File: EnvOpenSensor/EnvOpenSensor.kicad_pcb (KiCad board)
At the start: 2 copper layers, 89.7 x 67.5 mm, 76 parts, among them IC1 IS31FL3730-QFLS2-TR, IC2 IS31FL3730-QFLS2-TR, IC3 IS31FL3730-QFLS2-TR, IC4 IS31FL3730-QFLS2-TR, J1 HRO_TYPE-C-31-M-12, J2 AVR-ISP-6, SW1 SW_Push, SW2 SW_Push, SW3 SW_Push, SW4 SW_Push, U0 TCA9548ARGER, U1 SCD41-D-R2, U2 Si7021-A20, U4 ATtiny85-20S, U5 TPS63001DRCR

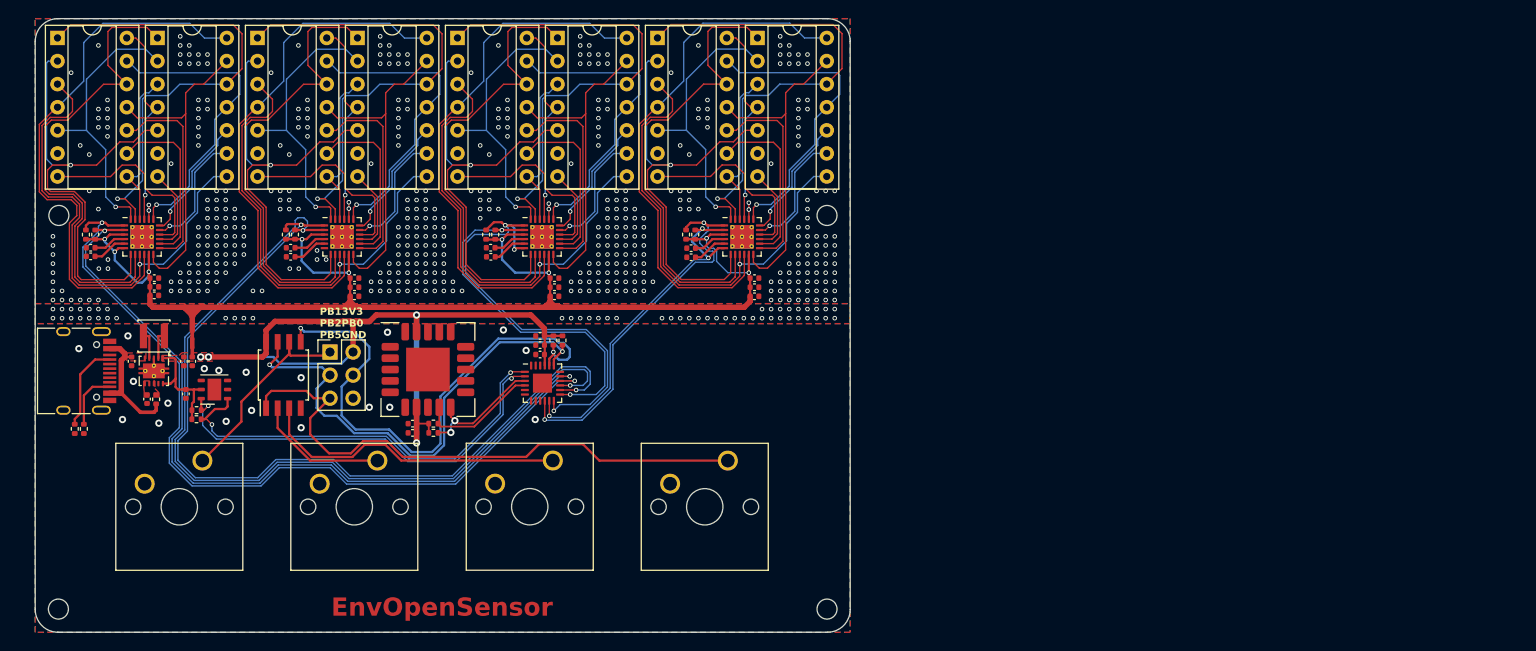
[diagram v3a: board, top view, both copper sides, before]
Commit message: recognised issues with the design, redid schematic to include onboard LEDs and a RP2040, started re-work on PCB
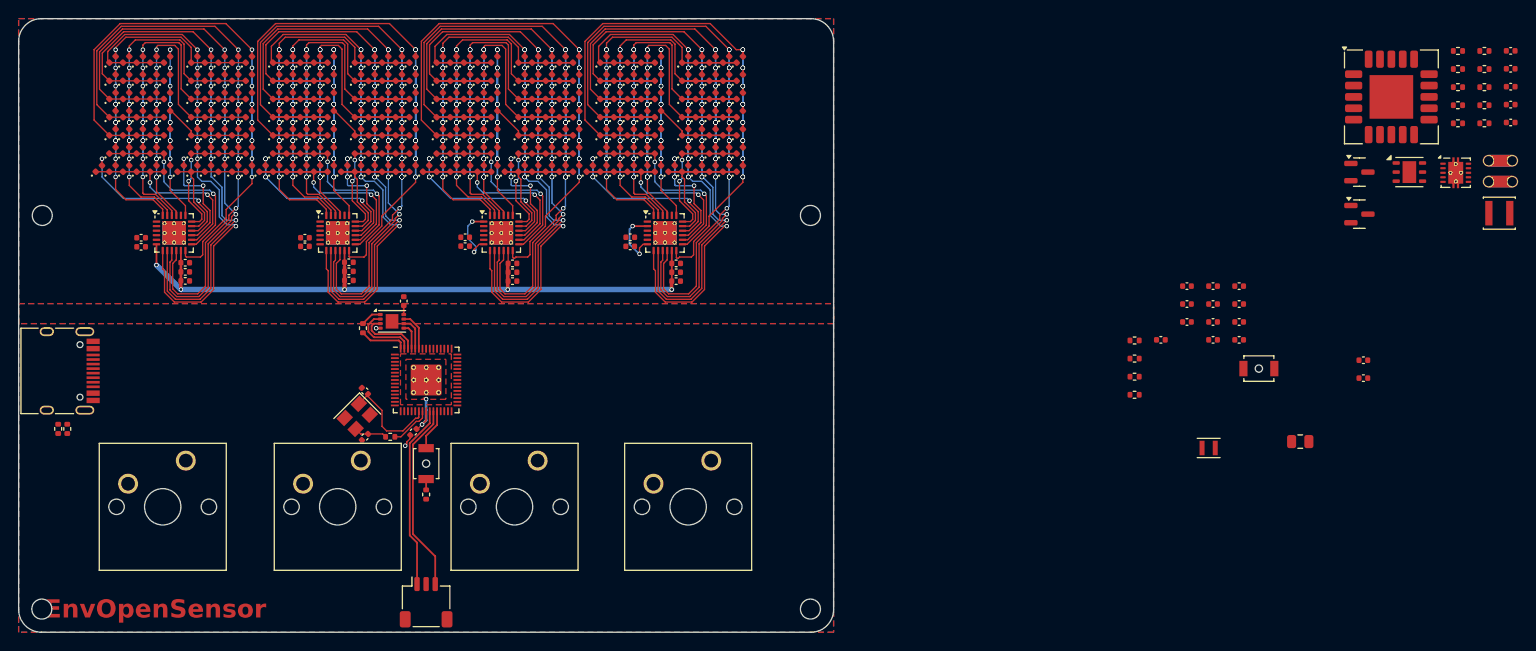
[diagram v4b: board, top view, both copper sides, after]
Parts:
- removed C101, C104, C107, C110: 0402 0.1uF, Capacitor_SMD:C_0402_1005Metric
- removed C102, C105, C108, C111: 0402 1uF, Capacitor_SMD:C_0402_1005Metric
- removed C103, C106, C109, C112: 0402 10uF, Capacitor_SMD:C_0402_1005Metric
- removed DIY-305-1, DIY-305-2, DIY-305-3, DIY-305-4, DIY-305-5, DIY-305-6, DIY-305-7, DIY-305-8: Dip-14 Socket, Package_DIP:DIP-14_W7.62mm_Socket
- removed NT0: NetTie_2, NetTie:NetTie-2_SMD_Pad0.5mm
- removed R101, R102, R103, R104, R105, R106, R107, R108, R14, R15, R16: 10K 0402, Resistor_SMD:R_0402_1005Metric
- removed U0: TCA9548ARGER, Package_DFN_QFN:Texas_RGE0024C_EP2.1x2.1mm
- added C19: 0402 0.1uF, Capacitor_SMD:C_0402_1005Metric, F.Cu at (62.3, 37.5)
- added C20: 0402 0.22uF, Capacitor_SMD:C_0402_1005Metric, F.Cu at (62.3, 36.5)
- added C21: 0402 1uF, Capacitor_SMD:C_0402_1005Metric, F.Cu at (67.5, 40.4)
- added C22: 0402 10uF, Capacitor_SMD:C_0402_1005Metric, F.Cu at (67.5, 41.4)
- added C23: 0402 0.1uF, Capacitor_SMD:C_0402_1005Metric, F.Cu at (85.5, 39.4)
- added C24: 0402 0.1uF, Capacitor_SMD:C_0402_1005Metric, F.Cu at (80.5, 37.5)
- added C25: 0402 0.22uF, Capacitor_SMD:C_0402_1005Metric, F.Cu at (80.5, 36.5)
- added C26: 0402 1uF, Capacitor_SMD:C_0402_1005Metric, F.Cu at (85.5, 40.4)
- added C27: 0402 10uF, Capacitor_SMD:C_0402_1005Metric, F.Cu at (85.5, 41.4)
- added C28: 15pf 0402, Capacitor_SMD:C_0402_1005Metric, F.Cu at (51.3, 53.5)
- added C29: 15pf 0402, Capacitor_SMD:C_0402_1005Metric, F.Cu at (51.3, 58.5)
- added C30: 100nf 0402, Capacitor_SMD:C_0402_1005Metric, F.Cu at (55.5, 43.6)
- added C31: 4.7uf 0402, Capacitor_SMD:C_0402_1005Metric, F.Cu at (138.8, 47.8)
- added C32: 4.7uf 0402, Capacitor_SMD:C_0402_1005Metric, F.Cu at (141.7, 41.9)
- added C33: 100nf 0402, Capacitor_SMD:C_0402_1005Metric, F.Cu at (141.7, 43.9)
- added C34: 4.7uf 0402, Capacitor_SMD:C_0402_1005Metric, F.Cu at (141.7, 45.9)
- added C35: 4.7uf 0402, Capacitor_SMD:C_0402_1005Metric, F.Cu at (56.6, 58.0)
- added C36: 100nf 0402, Capacitor_SMD:C_0402_1005Metric, F.Cu at (144.6, 41.9)
- added C37: 100nf 0402, Capacitor_SMD:C_0402_1005Metric, F.Cu at (144.6, 43.9)
- added C38: 100nf 0402, Capacitor_SMD:C_0402_1005Metric, F.Cu at (144.6, 45.9)
- added C39: 100nf 0402, Capacitor_SMD:C_0402_1005Metric, F.Cu at (144.6, 47.8)
- added C40: 100nf 0402, Capacitor_SMD:C_0402_1005Metric, F.Cu at (147.4, 41.9)
- added C41: 100nf 0402, Capacitor_SMD:C_0402_1005Metric, F.Cu at (147.4, 43.9)
- added C42: 100nf 0402, Capacitor_SMD:C_0402_1005Metric, F.Cu at (147.4, 45.9)
- added C43: 100nf 0402, Capacitor_SMD:C_0402_1005Metric, F.Cu at (147.4, 47.8)
- added C44: 10uf 0805, Capacitor_SMD:C_0805_2012Metric, F.Cu at (154.2, 59.0)
- added D1: LED 0402 10mA, LED_SMD:LED_0402_1005Metric, F.Cu at (22.0, 29.0)
- added D10: LED 0402 10mA, LED_SMD:LED_0402_1005Metric, F.Cu at (25.0, 19.0)
- added D100: LED 0402 10mA, LED_SMD:LED_0402_1005Metric, F.Cu at (46.0, 27.0)
- added D101: LED 0402 10mA, LED_SMD:LED_0402_1005Metric, F.Cu at (46.0, 29.0)
- added D102: LED 0402 10mA, LED_SMD:LED_0402_1005Metric, F.Cu at (47.5, 17.0)
- added D103: LED 0402 10mA, LED_SMD:LED_0402_1005Metric, F.Cu at (47.5, 19.0)
- added D104: LED 0402 10mA, LED_SMD:LED_0402_1005Metric, F.Cu at (47.5, 21.0)
- added D105: LED 0402 10mA, LED_SMD:LED_0402_1005Metric, F.Cu at (47.5, 23.0)
- added D106: LED 0402 10mA, LED_SMD:LED_0402_1005Metric, F.Cu at (47.5, 25.0)
- added D107: LED 0402 10mA, LED_SMD:LED_0402_1005Metric, F.Cu at (47.5, 27.0)
- added D108: LED 0402 10mA, LED_SMD:LED_0402_1005Metric, F.Cu at (47.5, 29.0)
- added D109: LED 0402 10mA, LED_SMD:LED_0402_1005Metric, F.Cu at (49.0, 29.0)
- added D11: LED 0402 10mA, LED_SMD:LED_0402_1005Metric, F.Cu at (25.0, 21.0)
- added D110: LED 0402 10mA, LED_SMD:LED_0402_1005Metric, F.Cu at (50.5, 17.0)
- added D111: LED 0402 10mA, LED_SMD:LED_0402_1005Metric, F.Cu at (50.5, 19.0)
- added D112: LED 0402 10mA, LED_SMD:LED_0402_1005Metric, F.Cu at (50.5, 21.0)
- added D113: LED 0402 10mA, LED_SMD:LED_0402_1005Metric, F.Cu at (50.5, 23.0)
- added D114: LED 0402 10mA, LED_SMD:LED_0402_1005Metric, F.Cu at (50.5, 25.0)
- added D115: LED 0402 10mA, LED_SMD:LED_0402_1005Metric, F.Cu at (50.5, 27.0)
- added D116: LED 0402 10mA, LED_SMD:LED_0402_1005Metric, F.Cu at (50.5, 29.0)
- added D117: LED 0402 10mA, LED_SMD:LED_0402_1005Metric, F.Cu at (52.0, 17.0)
- added D118: LED 0402 10mA, LED_SMD:LED_0402_1005Metric, F.Cu at (52.0, 19.0)
- added D119: LED 0402 10mA, LED_SMD:LED_0402_1005Metric, F.Cu at (52.0, 21.0)
- added D12: LED 0402 10mA, LED_SMD:LED_0402_1005Metric, F.Cu at (25.0, 23.0)
- added D120: LED 0402 10mA, LED_SMD:LED_0402_1005Metric, F.Cu at (52.0, 23.0)
- added D121: LED 0402 10mA, LED_SMD:LED_0402_1005Metric, F.Cu at (52.0, 25.0)
- added D122: LED 0402 10mA, LED_SMD:LED_0402_1005Metric, F.Cu at (52.0, 27.0)
- added D123: LED 0402 10mA, LED_SMD:LED_0402_1005Metric, F.Cu at (52.0, 29.0)
- added D124: LED 0402 10mA, LED_SMD:LED_0402_1005Metric, F.Cu at (53.5, 17.0)
- added D125: LED 0402 10mA, LED_SMD:LED_0402_1005Metric, F.Cu at (53.5, 19.0)
- added D126: LED 0402 10mA, LED_SMD:LED_0402_1005Metric, F.Cu at (53.5, 21.0)
- added D127: LED 0402 10mA, LED_SMD:LED_0402_1005Metric, F.Cu at (53.5, 23.0)
- added D128: LED 0402 10mA, LED_SMD:LED_0402_1005Metric, F.Cu at (53.5, 25.0)
- added D129: LED 0402 10mA, LED_SMD:LED_0402_1005Metric, F.Cu at (53.5, 27.0)
- added D13: LED 0402 10mA, LED_SMD:LED_0402_1005Metric, F.Cu at (25.0, 25.0)
- added D130: LED 0402 10mA, LED_SMD:LED_0402_1005Metric, F.Cu at (53.5, 29.0)
- added D131: LED 0402 10mA, LED_SMD:LED_0402_1005Metric, F.Cu at (55.0, 17.0)
- added D132: LED 0402 10mA, LED_SMD:LED_0402_1005Metric, F.Cu at (55.0, 19.0)
- added D133: LED 0402 10mA, LED_SMD:LED_0402_1005Metric, F.Cu at (55.0, 21.0)
- added D134: LED 0402 10mA, LED_SMD:LED_0402_1005Metric, F.Cu at (55.0, 23.0)
- added D135: LED 0402 10mA, LED_SMD:LED_0402_1005Metric, F.Cu at (55.0, 25.0)
- added D136: LED 0402 10mA, LED_SMD:LED_0402_1005Metric, F.Cu at (55.0, 27.0)
- added D137: LED 0402 10mA, LED_SMD:LED_0402_1005Metric, F.Cu at (55.0, 29.0)
- added D138: LED 0402 10mA, LED_SMD:LED_0402_1005Metric, F.Cu at (56.5, 17.0)
- added D139: LED 0402 10mA, LED_SMD:LED_0402_1005Metric, F.Cu at (56.5, 19.0)
- added D14: LED 0402 10mA, LED_SMD:LED_0402_1005Metric, F.Cu at (25.0, 27.0)
- added D140: LED 0402 10mA, LED_SMD:LED_0402_1005Metric, F.Cu at (56.5, 21.0)
- added D141: LED 0402 10mA, LED_SMD:LED_0402_1005Metric, F.Cu at (56.5, 23.0)
- added D142: LED 0402 10mA, LED_SMD:LED_0402_1005Metric, F.Cu at (56.5, 25.0)
- added D143: LED 0402 10mA, LED_SMD:LED_0402_1005Metric, F.Cu at (56.5, 27.0)
- added D144: LED 0402 10mA, LED_SMD:LED_0402_1005Metric, F.Cu at (56.5, 29.0)
- added D145: LED 0402 10mA, LED_SMD:LED_0402_1005Metric, F.Cu at (58.0, 29.0)
- added D146: LED 0402 10mA, LED_SMD:LED_0402_1005Metric, F.Cu at (59.5, 17.0)
- added D147: LED 0402 10mA, LED_SMD:LED_0402_1005Metric, F.Cu at (59.5, 19.0)
- added D148: LED 0402 10mA, LED_SMD:LED_0402_1005Metric, F.Cu at (59.5, 21.0)
- added D149: LED 0402 10mA, LED_SMD:LED_0402_1005Metric, F.Cu at (59.5, 23.0)
- added D15: LED 0402 10mA, LED_SMD:LED_0402_1005Metric, F.Cu at (25.0, 29.0)
- added D150: LED 0402 10mA, LED_SMD:LED_0402_1005Metric, F.Cu at (59.5, 25.0)
- added D151: LED 0402 10mA, LED_SMD:LED_0402_1005Metric, F.Cu at (59.5, 27.0)
- added D152: LED 0402 10mA, LED_SMD:LED_0402_1005Metric, F.Cu at (59.5, 29.0)
- added D153: LED 0402 10mA, LED_SMD:LED_0402_1005Metric, F.Cu at (61.0, 17.0)
- added D154: LED 0402 10mA, LED_SMD:LED_0402_1005Metric, F.Cu at (61.0, 19.0)
- added D155: LED 0402 10mA, LED_SMD:LED_0402_1005Metric, F.Cu at (61.0, 21.0)
- added D156: LED 0402 10mA, LED_SMD:LED_0402_1005Metric, F.Cu at (61.0, 23.0)
- added D157: LED 0402 10mA, LED_SMD:LED_0402_1005Metric, F.Cu at (61.0, 25.0)
- added D158: LED 0402 10mA, LED_SMD:LED_0402_1005Metric, F.Cu at (61.0, 27.0)
- added D159: LED 0402 10mA, LED_SMD:LED_0402_1005Metric, F.Cu at (61.0, 29.0)
- added D16: LED 0402 10mA, LED_SMD:LED_0402_1005Metric, F.Cu at (26.5, 17.0)
- added D160: LED 0402 10mA, LED_SMD:LED_0402_1005Metric, F.Cu at (62.5, 17.0)
- added D161: LED 0402 10mA, LED_SMD:LED_0402_1005Metric, F.Cu at (62.5, 19.0)
- added D162: LED 0402 10mA, LED_SMD:LED_0402_1005Metric, F.Cu at (62.5, 21.0)
- added D163: LED 0402 10mA, LED_SMD:LED_0402_1005Metric, F.Cu at (62.5, 23.0)
- added D164: LED 0402 10mA, LED_SMD:LED_0402_1005Metric, F.Cu at (62.5, 25.0)
- added D165: LED 0402 10mA, LED_SMD:LED_0402_1005Metric, F.Cu at (62.5, 27.0)
- added D166: LED 0402 10mA, LED_SMD:LED_0402_1005Metric, F.Cu at (62.5, 29.0)
- added D167: LED 0402 10mA, LED_SMD:LED_0402_1005Metric, F.Cu at (64.0, 17.0)
- added D168: LED 0402 10mA, LED_SMD:LED_0402_1005Metric, F.Cu at (64.0, 19.0)
- added D169: LED 0402 10mA, LED_SMD:LED_0402_1005Metric, F.Cu at (64.0, 21.0)
- added D17: LED 0402 10mA, LED_SMD:LED_0402_1005Metric, F.Cu at (26.5, 19.0)
- added D170: LED 0402 10mA, LED_SMD:LED_0402_1005Metric, F.Cu at (64.0, 23.0)
- added D171: LED 0402 10mA, LED_SMD:LED_0402_1005Metric, F.Cu at (64.0, 25.0)
- added D172: LED 0402 10mA, LED_SMD:LED_0402_1005Metric, F.Cu at (64.0, 27.0)
- added D173: LED 0402 10mA, LED_SMD:LED_0402_1005Metric, F.Cu at (64.0, 29.0)
- added D174: LED 0402 10mA, LED_SMD:LED_0402_1005Metric, F.Cu at (65.5, 17.0)
- added D175: LED 0402 10mA, LED_SMD:LED_0402_1005Metric, F.Cu at (65.5, 19.0)
- added D176: LED 0402 10mA, LED_SMD:LED_0402_1005Metric, F.Cu at (65.5, 21.0)
- added D177: LED 0402 10mA, LED_SMD:LED_0402_1005Metric, F.Cu at (65.5, 23.0)
- added D178: LED 0402 10mA, LED_SMD:LED_0402_1005Metric, F.Cu at (65.5, 25.0)
- added D179: LED 0402 10mA, LED_SMD:LED_0402_1005Metric, F.Cu at (65.5, 27.0)
- added D18: LED 0402 10mA, LED_SMD:LED_0402_1005Metric, F.Cu at (26.5, 21.0)
- added D180: LED 0402 10mA, LED_SMD:LED_0402_1005Metric, F.Cu at (65.5, 29.0)
- added D181: LED 0402 10mA, LED_SMD:LED_0402_1005Metric, F.Cu at (67.0, 29.0)
- added D182: LED 0402 10mA, LED_SMD:LED_0402_1005Metric, F.Cu at (68.5, 17.0)
- added D183: LED 0402 10mA, LED_SMD:LED_0402_1005Metric, F.Cu at (68.5, 19.0)
- added D184: LED 0402 10mA, LED_SMD:LED_0402_1005Metric, F.Cu at (68.5, 21.0)
- added D185: LED 0402 10mA, LED_SMD:LED_0402_1005Metric, F.Cu at (68.5, 23.0)
- added D186: LED 0402 10mA, LED_SMD:LED_0402_1005Metric, F.Cu at (68.5, 25.0)
- added D187: LED 0402 10mA, LED_SMD:LED_0402_1005Metric, F.Cu at (68.5, 27.0)
- added D188: LED 0402 10mA, LED_SMD:LED_0402_1005Metric, F.Cu at (68.5, 29.0)
- added D189: LED 0402 10mA, LED_SMD:LED_0402_1005Metric, F.Cu at (70.0, 17.0)
- added D19: LED 0402 10mA, LED_SMD:LED_0402_1005Metric, F.Cu at (26.5, 23.0)
- added D190: LED 0402 10mA, LED_SMD:LED_0402_1005Metric, F.Cu at (70.0, 19.0)
- added D191: LED 0402 10mA, LED_SMD:LED_0402_1005Metric, F.Cu at (70.0, 21.0)
- added D192: LED 0402 10mA, LED_SMD:LED_0402_1005Metric, F.Cu at (70.0, 23.0)
- added D193: LED 0402 10mA, LED_SMD:LED_0402_1005Metric, F.Cu at (70.0, 25.0)
- added D194: LED 0402 10mA, LED_SMD:LED_0402_1005Metric, F.Cu at (70.0, 27.0)
- added D195: LED 0402 10mA, LED_SMD:LED_0402_1005Metric, F.Cu at (70.0, 29.0)
- added D196: LED 0402 10mA, LED_SMD:LED_0402_1005Metric, F.Cu at (71.5, 17.0)
- added D197: LED 0402 10mA, LED_SMD:LED_0402_1005Metric, F.Cu at (71.5, 19.0)
- added D198: LED 0402 10mA, LED_SMD:LED_0402_1005Metric, F.Cu at (71.5, 21.0)
- added D199: LED 0402 10mA, LED_SMD:LED_0402_1005Metric, F.Cu at (71.5, 23.0)
- added D2: LED 0402 10mA, LED_SMD:LED_0402_1005Metric, F.Cu at (23.5, 17.0)
- added D20: LED 0402 10mA, LED_SMD:LED_0402_1005Metric, F.Cu at (26.5, 25.0)
- added D200: LED 0402 10mA, LED_SMD:LED_0402_1005Metric, F.Cu at (71.5, 25.0)
- added D201: LED 0402 10mA, LED_SMD:LED_0402_1005Metric, F.Cu at (71.5, 27.0)
- added D202: LED 0402 10mA, LED_SMD:LED_0402_1005Metric, F.Cu at (71.5, 29.0)
- added D203: LED 0402 10mA, LED_SMD:LED_0402_1005Metric, F.Cu at (73.0, 17.0)
- added D204: LED 0402 10mA, LED_SMD:LED_0402_1005Metric, F.Cu at (73.0, 19.0)
- added D205: LED 0402 10mA, LED_SMD:LED_0402_1005Metric, F.Cu at (73.0, 21.0)
- added D206: LED 0402 10mA, LED_SMD:LED_0402_1005Metric, F.Cu at (73.0, 23.0)
- added D207: LED 0402 10mA, LED_SMD:LED_0402_1005Metric, F.Cu at (73.0, 25.0)
- added D208: LED 0402 10mA, LED_SMD:LED_0402_1005Metric, F.Cu at (73.0, 27.0)
- added D209: LED 0402 10mA, LED_SMD:LED_0402_1005Metric, F.Cu at (73.0, 29.0)
- added D21: LED 0402 10mA, LED_SMD:LED_0402_1005Metric, F.Cu at (26.5, 27.0)
- added D210: LED 0402 10mA, LED_SMD:LED_0402_1005Metric, F.Cu at (74.5, 17.0)
- added D211: LED 0402 10mA, LED_SMD:LED_0402_1005Metric, F.Cu at (74.5, 19.0)
- added D212: LED 0402 10mA, LED_SMD:LED_0402_1005Metric, F.Cu at (74.5, 21.0)
- added D213: LED 0402 10mA, LED_SMD:LED_0402_1005Metric, F.Cu at (74.5, 23.0)
- added D214: LED 0402 10mA, LED_SMD:LED_0402_1005Metric, F.Cu at (74.5, 25.0)
- added D215: LED 0402 10mA, LED_SMD:LED_0402_1005Metric, F.Cu at (74.5, 27.0)
- added D216: LED 0402 10mA, LED_SMD:LED_0402_1005Metric, F.Cu at (74.5, 29.0)
- added D217: LED 0402 10mA, LED_SMD:LED_0402_1005Metric, F.Cu at (76.0, 29.0)
- added D218: LED 0402 10mA, LED_SMD:LED_0402_1005Metric, F.Cu at (77.5, 17.0)
- added D219: LED 0402 10mA, LED_SMD:LED_0402_1005Metric, F.Cu at (77.5, 19.0)
- added D22: LED 0402 10mA, LED_SMD:LED_0402_1005Metric, F.Cu at (26.5, 29.0)
- added D220: LED 0402 10mA, LED_SMD:LED_0402_1005Metric, F.Cu at (77.5, 21.0)
- added D221: LED 0402 10mA, LED_SMD:LED_0402_1005Metric, F.Cu at (77.5, 23.0)
- added D222: LED 0402 10mA, LED_SMD:LED_0402_1005Metric, F.Cu at (77.5, 25.0)
- added D223: LED 0402 10mA, LED_SMD:LED_0402_1005Metric, F.Cu at (77.5, 27.0)
- added D224: LED 0402 10mA, LED_SMD:LED_0402_1005Metric, F.Cu at (77.5, 29.0)
- added D225: LED 0402 10mA, LED_SMD:LED_0402_1005Metric, F.Cu at (79.0, 17.0)
- added D226: LED 0402 10mA, LED_SMD:LED_0402_1005Metric, F.Cu at (79.0, 19.0)
- added D227: LED 0402 10mA, LED_SMD:LED_0402_1005Metric, F.Cu at (79.0, 21.0)
- added D228: LED 0402 10mA, LED_SMD:LED_0402_1005Metric, F.Cu at (79.0, 23.0)
- added D229: LED 0402 10mA, LED_SMD:LED_0402_1005Metric, F.Cu at (79.0, 25.0)
- added D23: LED 0402 10mA, LED_SMD:LED_0402_1005Metric, F.Cu at (28.0, 17.0)
- added D230: LED 0402 10mA, LED_SMD:LED_0402_1005Metric, F.Cu at (79.0, 27.0)
- added D231: LED 0402 10mA, LED_SMD:LED_0402_1005Metric, F.Cu at (79.0, 29.0)
- added D232: LED 0402 10mA, LED_SMD:LED_0402_1005Metric, F.Cu at (80.5, 17.0)
- added D233: LED 0402 10mA, LED_SMD:LED_0402_1005Metric, F.Cu at (80.5, 19.0)
- added D234: LED 0402 10mA, LED_SMD:LED_0402_1005Metric, F.Cu at (80.5, 21.0)
- added D235: LED 0402 10mA, LED_SMD:LED_0402_1005Metric, F.Cu at (80.5, 23.0)
- added D236: LED 0402 10mA, LED_SMD:LED_0402_1005Metric, F.Cu at (80.5, 25.0)
- added D237: LED 0402 10mA, LED_SMD:LED_0402_1005Metric, F.Cu at (80.5, 27.0)
- added D238: LED 0402 10mA, LED_SMD:LED_0402_1005Metric, F.Cu at (80.5, 29.0)
- added D239: LED 0402 10mA, LED_SMD:LED_0402_1005Metric, F.Cu at (82.0, 17.0)
- added D24: LED 0402 10mA, LED_SMD:LED_0402_1005Metric, F.Cu at (28.0, 19.0)
- added D240: LED 0402 10mA, LED_SMD:LED_0402_1005Metric, F.Cu at (82.0, 19.0)
- added D241: LED 0402 10mA, LED_SMD:LED_0402_1005Metric, F.Cu at (82.0, 21.0)
- added D242: LED 0402 10mA, LED_SMD:LED_0402_1005Metric, F.Cu at (82.0, 23.0)
- added D243: LED 0402 10mA, LED_SMD:LED_0402_1005Metric, F.Cu at (82.0, 25.0)
- added D244: LED 0402 10mA, LED_SMD:LED_0402_1005Metric, F.Cu at (82.0, 27.0)
- added D245: LED 0402 10mA, LED_SMD:LED_0402_1005Metric, F.Cu at (82.0, 29.0)
- added D246: LED 0402 10mA, LED_SMD:LED_0402_1005Metric, F.Cu at (83.5, 17.0)
- added D247: LED 0402 10mA, LED_SMD:LED_0402_1005Metric, F.Cu at (83.5, 19.0)
- added D248: LED 0402 10mA, LED_SMD:LED_0402_1005Metric, F.Cu at (83.5, 21.0)
- added D249: LED 0402 10mA, LED_SMD:LED_0402_1005Metric, F.Cu at (83.5, 23.0)
- added D25: LED 0402 10mA, LED_SMD:LED_0402_1005Metric, F.Cu at (28.0, 21.0)
- added D250: LED 0402 10mA, LED_SMD:LED_0402_1005Metric, F.Cu at (83.5, 25.0)
- added D251: LED 0402 10mA, LED_SMD:LED_0402_1005Metric, F.Cu at (83.5, 27.0)
- added D252: LED 0402 10mA, LED_SMD:LED_0402_1005Metric, F.Cu at (83.5, 29.0)
- added D253: LED 0402 10mA, LED_SMD:LED_0402_1005Metric, F.Cu at (85.0, 29.0)
- added D254: LED 0402 10mA, LED_SMD:LED_0402_1005Metric, F.Cu at (86.5, 17.0)
- added D255: LED 0402 10mA, LED_SMD:LED_0402_1005Metric, F.Cu at (86.5, 19.0)
- added D256: LED 0402 10mA, LED_SMD:LED_0402_1005Metric, F.Cu at (86.5, 21.0)
- added D257: LED 0402 10mA, LED_SMD:LED_0402_1005Metric, F.Cu at (86.5, 23.0)
- added D258: LED 0402 10mA, LED_SMD:LED_0402_1005Metric, F.Cu at (86.5, 25.0)
- added D259: LED 0402 10mA, LED_SMD:LED_0402_1005Metric, F.Cu at (86.5, 27.0)
- added D26: LED 0402 10mA, LED_SMD:LED_0402_1005Metric, F.Cu at (28.0, 23.0)
- added D260: LED 0402 10mA, LED_SMD:LED_0402_1005Metric, F.Cu at (86.5, 29.0)
- added D261: LED 0402 10mA, LED_SMD:LED_0402_1005Metric, F.Cu at (88.0, 17.0)
- added D262: LED 0402 10mA, LED_SMD:LED_0402_1005Metric, F.Cu at (88.0, 19.0)
- added D263: LED 0402 10mA, LED_SMD:LED_0402_1005Metric, F.Cu at (88.0, 21.0)
- added D264: LED 0402 10mA, LED_SMD:LED_0402_1005Metric, F.Cu at (88.0, 23.0)
- added D265: LED 0402 10mA, LED_SMD:LED_0402_1005Metric, F.Cu at (88.0, 25.0)
- added D266: LED 0402 10mA, LED_SMD:LED_0402_1005Metric, F.Cu at (88.0, 27.0)
- added D267: LED 0402 10mA, LED_SMD:LED_0402_1005Metric, F.Cu at (88.0, 29.0)
- added D268: LED 0402 10mA, LED_SMD:LED_0402_1005Metric, F.Cu at (89.5, 17.0)
- added D269: LED 0402 10mA, LED_SMD:LED_0402_1005Metric, F.Cu at (89.5, 19.0)
- added D27: LED 0402 10mA, LED_SMD:LED_0402_1005Metric, F.Cu at (28.0, 25.0)
- added D270: LED 0402 10mA, LED_SMD:LED_0402_1005Metric, F.Cu at (89.5, 21.0)
- added D271: LED 0402 10mA, LED_SMD:LED_0402_1005Metric, F.Cu at (89.5, 23.0)
- added D272: LED 0402 10mA, LED_SMD:LED_0402_1005Metric, F.Cu at (89.5, 25.0)
- added D273: LED 0402 10mA, LED_SMD:LED_0402_1005Metric, F.Cu at (89.5, 27.0)
- added D274: LED 0402 10mA, LED_SMD:LED_0402_1005Metric, F.Cu at (89.5, 29.0)
- added D275: LED 0402 10mA, LED_SMD:LED_0402_1005Metric, F.Cu at (91.0, 17.0)
- added D276: LED 0402 10mA, LED_SMD:LED_0402_1005Metric, F.Cu at (91.0, 19.0)
- added D277: LED 0402 10mA, LED_SMD:LED_0402_1005Metric, F.Cu at (91.0, 21.0)
- added D278: LED 0402 10mA, LED_SMD:LED_0402_1005Metric, F.Cu at (91.0, 23.0)
- added D279: LED 0402 10mA, LED_SMD:LED_0402_1005Metric, F.Cu at (91.0, 25.0)
- added D28: LED 0402 10mA, LED_SMD:LED_0402_1005Metric, F.Cu at (28.0, 27.0)
- added D280: LED 0402 10mA, LED_SMD:LED_0402_1005Metric, F.Cu at (91.0, 27.0)
- added D281: LED 0402 10mA, LED_SMD:LED_0402_1005Metric, F.Cu at (91.0, 29.0)
- added D282: LED 0402 10mA, LED_SMD:LED_0402_1005Metric, F.Cu at (92.5, 17.0)
- added D283: LED 0402 10mA, LED_SMD:LED_0402_1005Metric, F.Cu at (92.5, 19.0)
- added D284: LED 0402 10mA, LED_SMD:LED_0402_1005Metric, F.Cu at (92.5, 21.0)
- added D285: LED 0402 10mA, LED_SMD:LED_0402_1005Metric, F.Cu at (92.5, 23.0)
- added D286: LED 0402 10mA, LED_SMD:LED_0402_1005Metric, F.Cu at (92.5, 25.0)
- added D287: LED 0402 10mA, LED_SMD:LED_0402_1005Metric, F.Cu at (92.5, 27.0)
- added D288: LED 0402 10mA, LED_SMD:LED_0402_1005Metric, F.Cu at (92.5, 29.0)
- added D29: LED 0402 10mA, LED_SMD:LED_0402_1005Metric, F.Cu at (28.0, 29.0)
- added D3: LED 0402 10mA, LED_SMD:LED_0402_1005Metric, F.Cu at (23.5, 19.0)
- added D30: LED 0402 10mA, LED_SMD:LED_0402_1005Metric, F.Cu at (29.5, 17.0)
- added D31: LED 0402 10mA, LED_SMD:LED_0402_1005Metric, F.Cu at (29.5, 19.0)
- added D32: LED 0402 10mA, LED_SMD:LED_0402_1005Metric, F.Cu at (29.5, 21.0)
- added D33: LED 0402 10mA, LED_SMD:LED_0402_1005Metric, F.Cu at (29.5, 23.0)
- added D34: LED 0402 10mA, LED_SMD:LED_0402_1005Metric, F.Cu at (29.5, 25.0)
- added D35: LED 0402 10mA, LED_SMD:LED_0402_1005Metric, F.Cu at (29.5, 27.0)
- added D36: LED 0402 10mA, LED_SMD:LED_0402_1005Metric, F.Cu at (29.5, 29.0)
- added D37: LED 0402 10mA, LED_SMD:LED_0402_1005Metric, F.Cu at (31.0, 29.0)
- added D38: LED 0402 10mA, LED_SMD:LED_0402_1005Metric, F.Cu at (32.5, 17.0)
- added D39: LED 0402 10mA, LED_SMD:LED_0402_1005Metric, F.Cu at (32.5, 19.0)
- added D4: LED 0402 10mA, LED_SMD:LED_0402_1005Metric, F.Cu at (23.5, 21.0)
- added D40: LED 0402 10mA, LED_SMD:LED_0402_1005Metric, F.Cu at (32.5, 21.0)
- added D41: LED 0402 10mA, LED_SMD:LED_0402_1005Metric, F.Cu at (32.5, 23.0)
- added D42: LED 0402 10mA, LED_SMD:LED_0402_1005Metric, F.Cu at (32.5, 25.0)
- added D43: LED 0402 10mA, LED_SMD:LED_0402_1005Metric, F.Cu at (32.5, 27.0)
- added D44: LED 0402 10mA, LED_SMD:LED_0402_1005Metric, F.Cu at (32.5, 29.0)
- added D45: LED 0402 10mA, LED_SMD:LED_0402_1005Metric, F.Cu at (34.0, 17.0)
- added D46: LED 0402 10mA, LED_SMD:LED_0402_1005Metric, F.Cu at (34.0, 19.0)
- added D47: LED 0402 10mA, LED_SMD:LED_0402_1005Metric, F.Cu at (34.0, 21.0)
- added D48: LED 0402 10mA, LED_SMD:LED_0402_1005Metric, F.Cu at (34.0, 23.0)
- added D49: LED 0402 10mA, LED_SMD:LED_0402_1005Metric, F.Cu at (34.0, 25.0)
- added D5: LED 0402 10mA, LED_SMD:LED_0402_1005Metric, F.Cu at (23.5, 23.0)
- added D50: LED 0402 10mA, LED_SMD:LED_0402_1005Metric, F.Cu at (34.0, 27.0)
- added D51: LED 0402 10mA, LED_SMD:LED_0402_1005Metric, F.Cu at (34.0, 29.0)
- added D52: LED 0402 10mA, LED_SMD:LED_0402_1005Metric, F.Cu at (35.5, 17.0)
- added D53: LED 0402 10mA, LED_SMD:LED_0402_1005Metric, F.Cu at (35.5, 19.0)
- added D54: LED 0402 10mA, LED_SMD:LED_0402_1005Metric, F.Cu at (35.5, 21.0)
- added D55: LED 0402 10mA, LED_SMD:LED_0402_1005Metric, F.Cu at (35.5, 23.0)
- added D56: LED 0402 10mA, LED_SMD:LED_0402_1005Metric, F.Cu at (35.5, 25.0)
- added D57: LED 0402 10mA, LED_SMD:LED_0402_1005Metric, F.Cu at (35.5, 27.0)
- added D58: LED 0402 10mA, LED_SMD:LED_0402_1005Metric, F.Cu at (35.5, 29.0)
- added D59: LED 0402 10mA, LED_SMD:LED_0402_1005Metric, F.Cu at (37.0, 17.0)
- added D6: LED 0402 10mA, LED_SMD:LED_0402_1005Metric, F.Cu at (23.5, 25.0)
- added D60: LED 0402 10mA, LED_SMD:LED_0402_1005Metric, F.Cu at (37.0, 19.0)
- added D61: LED 0402 10mA, LED_SMD:LED_0402_1005Metric, F.Cu at (37.0, 21.0)
- added D62: LED 0402 10mA, LED_SMD:LED_0402_1005Metric, F.Cu at (37.0, 23.0)
- added D63: LED 0402 10mA, LED_SMD:LED_0402_1005Metric, F.Cu at (37.0, 25.0)
- added D64: LED 0402 10mA, LED_SMD:LED_0402_1005Metric, F.Cu at (37.0, 27.0)
- added D65: LED 0402 10mA, LED_SMD:LED_0402_1005Metric, F.Cu at (37.0, 29.0)
- added D66: LED 0402 10mA, LED_SMD:LED_0402_1005Metric, F.Cu at (38.5, 17.0)
- added D67: LED 0402 10mA, LED_SMD:LED_0402_1005Metric, F.Cu at (38.5, 19.0)
- added D68: LED 0402 10mA, LED_SMD:LED_0402_1005Metric, F.Cu at (38.5, 21.0)
- added D69: LED 0402 10mA, LED_SMD:LED_0402_1005Metric, F.Cu at (38.5, 23.0)
- added D7: LED 0402 10mA, LED_SMD:LED_0402_1005Metric, F.Cu at (23.5, 27.0)
- added D70: LED 0402 10mA, LED_SMD:LED_0402_1005Metric, F.Cu at (38.5, 25.0)
- added D71: LED 0402 10mA, LED_SMD:LED_0402_1005Metric, F.Cu at (38.5, 27.0)
- added D72: LED 0402 10mA, LED_SMD:LED_0402_1005Metric, F.Cu at (38.5, 29.0)
- added D73: LED 0402 10mA, LED_SMD:LED_0402_1005Metric, F.Cu at (40.0, 29.0)
- added D74: LED 0402 10mA, LED_SMD:LED_0402_1005Metric, F.Cu at (41.5, 17.0)
- added D75: LED 0402 10mA, LED_SMD:LED_0402_1005Metric, F.Cu at (41.5, 19.0)
- added D76: LED 0402 10mA, LED_SMD:LED_0402_1005Metric, F.Cu at (41.5, 21.0)
- added D77: LED 0402 10mA, LED_SMD:LED_0402_1005Metric, F.Cu at (41.5, 23.0)
- added D78: LED 0402 10mA, LED_SMD:LED_0402_1005Metric, F.Cu at (41.5, 25.0)
- added D79: LED 0402 10mA, LED_SMD:LED_0402_1005Metric, F.Cu at (41.5, 27.0)
- added D8: LED 0402 10mA, LED_SMD:LED_0402_1005Metric, F.Cu at (23.5, 29.0)
- added D80: LED 0402 10mA, LED_SMD:LED_0402_1005Metric, F.Cu at (41.5, 29.0)
- added D81: LED 0402 10mA, LED_SMD:LED_0402_1005Metric, F.Cu at (43.0, 17.0)
- added D82: LED 0402 10mA, LED_SMD:LED_0402_1005Metric, F.Cu at (43.0, 19.0)
- added D83: LED 0402 10mA, LED_SMD:LED_0402_1005Metric, F.Cu at (43.0, 21.0)
- added D84: LED 0402 10mA, LED_SMD:LED_0402_1005Metric, F.Cu at (43.0, 23.0)
- added D85: LED 0402 10mA, LED_SMD:LED_0402_1005Metric, F.Cu at (43.0, 25.0)
- added D86: LED 0402 10mA, LED_SMD:LED_0402_1005Metric, F.Cu at (43.0, 27.0)
- added D87: LED 0402 10mA, LED_SMD:LED_0402_1005Metric, F.Cu at (43.0, 29.0)
- added D88: LED 0402 10mA, LED_SMD:LED_0402_1005Metric, F.Cu at (44.5, 17.0)
- added D89: LED 0402 10mA, LED_SMD:LED_0402_1005Metric, F.Cu at (44.5, 19.0)
- added D9: LED 0402 10mA, LED_SMD:LED_0402_1005Metric, F.Cu at (25.0, 17.0)
- added D90: LED 0402 10mA, LED_SMD:LED_0402_1005Metric, F.Cu at (44.5, 21.0)
- added D91: LED 0402 10mA, LED_SMD:LED_0402_1005Metric, F.Cu at (44.5, 23.0)
- added D92: LED 0402 10mA, LED_SMD:LED_0402_1005Metric, F.Cu at (44.5, 25.0)
- added D93: LED 0402 10mA, LED_SMD:LED_0402_1005Metric, F.Cu at (44.5, 27.0)
- added D94: LED 0402 10mA, LED_SMD:LED_0402_1005Metric, F.Cu at (44.5, 29.0)
- added D95: LED 0402 10mA, LED_SMD:LED_0402_1005Metric, F.Cu at (46.0, 17.0)
- added D96: LED 0402 10mA, LED_SMD:LED_0402_1005Metric, F.Cu at (46.0, 19.0)
- added D97: LED 0402 10mA, LED_SMD:LED_0402_1005Metric, F.Cu at (46.0, 21.0)
- added D98: LED 0402 10mA, LED_SMD:LED_0402_1005Metric, F.Cu at (46.0, 23.0)
- added D99: LED 0402 10mA, LED_SMD:LED_0402_1005Metric, F.Cu at (46.0, 25.0)
- added L2: 3.3uf 2016, Inductor_SMD:L_Murata_DFE201610P, F.Cu at (144.1, 59.7)
- added NT1: NetTie_2, NetTie:NetTie-2_THT_Pad1.0mm, F.Cu at (174.9, 28.1)
- added NT2: NetTie_2, NetTie:NetTie-2_THT_Pad1.0mm, F.Cu at (174.9, 30.4)
- added Q1: BSS138, Package_TO_SOT_SMD:SOT-23, F.Cu at (160.7, 29.4)
- added Q2: BSS138, Package_TO_SOT_SMD:SOT-23, F.Cu at (160.7, 34.0)
- added R11: 10K 0402, Resistor_SMD:R_0402_1005Metric, F.Cu at (174.4, 20.0)
- added R12: 10K 0402, Resistor_SMD:R_0402_1005Metric, F.Cu at (174.4, 22.0)
- added R23: 0r 0402, Resistor_SMD:R_0402_1005Metric, F.Cu at (51.0, 46.5)
- added R25: 1k 4020, Resistor_SMD:R_0402_1005Metric, F.Cu at (54.0, 58.5)
- added R26: 1k 4020, Resistor_SMD:R_0402_1005Metric, F.Cu at (58.0, 64.8)
- added R27: 33r 0402, Resistor_SMD:R_0402_1005Metric, F.Cu at (135.9, 47.9)
- added R28: 1k 4020, Resistor_SMD:R_0402_1005Metric, F.Cu at (135.9, 49.9)
- added R29: 27r 0402, Resistor_SMD:R_0402_1005Metric, F.Cu at (135.9, 51.9)
- added R3: 5.1K 0402, Resistor_SMD:R_0402_1005Metric, F.Cu at (171.5, 16.1)
- added R30: 27r 0402, Resistor_SMD:R_0402_1005Metric, F.Cu at (135.9, 53.9)
- added R7: 100ohm 0402, Resistor_SMD:R_0402_1005Metric, F.Cu at (171.5, 24.0)
- added R8: 10K 0402, Resistor_SMD:R_0402_1005Metric, F.Cu at (174.4, 16.1)
- added R9: 10K 0402, Resistor_SMD:R_0402_1005Metric, F.Cu at (174.4, 18.0)
- added SW5: B3U-1000, Button_Switch_SMD:SW_SPST_B3U-1000P-B, F.Cu at (149.6, 51.0)
- added SW6: B3U-1000, Button_Switch_SMD:SW_SPST_B3U-1000P-B, F.Cu at (58.0, 61.5)
- added U3: SCD41-D-R2, Sensor:Sensirion_SCD4x-1EP_10.1x10.1mm_P1.25mm_EP4.8x4.8mm, F.Cu at (164.2, 21.1)
- added Y1: ABM8-272-T3, Crystal:Crystal_SMD_3225-4Pin_3.2x2.5mm, F.Cu at (50.4, 56.2)
- C1: value 10uF 0402 -> 0.1uF 0402
- C11: value 0402 0.22uF -> 0402 1uF
- C12: value 0402 0.22uF -> 0402 10uF
- C13: value 0402 0.22uF -> 0402 0.1uF
- C14: value 0402 1uF -> 0402 0.1uF
- C15: value 0402 10uF -> 0402 0.22uF
- C16: value 0402 0.1uF -> 0402 1uF
- C17: value 0402 1uF -> 0402 10uF
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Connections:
- C1 pad 1: VBUS -> +3V3
- C10 pad 2: Net-(IC2-IN) -> Net-(IC1-IN)
- C11 pad 1: GND -> VCC
- C11 pad 2: Net-(IC1-IN) -> GND
- C12 pad 1: GND -> VCC
- C12 pad 2: Net-(IC3-IN) -> GND
- C13 pad 1: GND -> VCC
- C13 pad 2: Net-(IC4-IN) -> GND
- C14 pad 1: +3V3 -> GND
- C14 pad 2: GND -> Net-(IC2-C_FILT)
- C15 pad 1: +3V3 -> GND
- C15 pad 2: GND -> Net-(IC2-IN)
- C16 pad 1: +3V3 -> VCC
- C17 pad 1: +3V3 -> VCC
- C18 pad 1: +3V3 -> VCC
- C2 pad 1: GND -> VBUS
- C2 pad 2: Net-(IC3-C_FILT) -> GND
- C3 pad 1: GND -> Net-(U2-EN)
- C3 pad 2: Net-(IC1-C_FILT) -> GND
- C5 pad 1: Net-(U5-EN) -> +3V3
- C6 pad 1: +3V3 -> +5V
- C7 pad 1: +3V3 -> +5V
- C8 pad 1: GND -> VCC
- C8 pad 2: Net-(IC2-C_FILT) -> GND
- C9 pad 2: Net-(IC4-C_FILT) -> Net-(IC1-C_FILT)
- IC1 pad 1: SDA7_3V3 -> I2C_SDA_5V0
- IC1 pad 2: SCL7_3V3 -> I2C_SCL_5V0
- IC2 pad 1: SDA6_3V3 -> I2C_SDA_5V0
- IC2 pad 2: SCL6_3V3 -> I2C_SCL_5V0
- IC3 pad 1: SDA5_3V3 -> I2C_SDA_5V0
- IC3 pad 2: SCL5_3V3 -> I2C_SCL_5V0
- IC3 pad 6: SDA5_3V3 -> I2C_SDA_5V0
- IC4 pad 1: SDA4_3V3 -> I2C_SDA_5V0
- IC4 pad 2: SCL4_3V3 -> I2C_SCL_5V0
- IC4 pad 6: SCL4_3V3 -> I2C_SCL_5V0
- J1 pad A6: unconnected-(J1-D+-PadA6) -> USB_D+
- J1 pad A7: unconnected-(J1-D--PadA7) -> USB_D-
- J1 pad B6: unconnected-(J1-D+-PadB6) -> USB_D+
- J1 pad B7: unconnected-(J1-D--PadB7) -> USB_D-
- J2 pad 1: PB1 -> /MCU/SWCLK
- J2 pad 2: +3V3 -> GND
- J2 pad 3: PB2 -> /MCU/SWD
- L1 pad 1: Net-(U5-L1) -> Net-(U2-L1)
- L1 pad 2: Net-(U5-L2) -> Net-(U2-L2)
- R1 pad 1: Net-(J1-CC1) -> SI_I2C_SDA_3V3
- R1 pad 2: GND -> +3V3
- R13 pad 1: SDA1_3V3 -> I2C_SDA_5V0
- R13 pad 2: +3V3 -> +5V
- R2 pad 1: Net-(J1-CC2) -> SI_I2C_SCL_3V3
- R2 pad 2: GND -> +3V3
- R4 pad 1: +3V3 -> Net-(J1-CC2)
- R4 pad 2: PB0 -> GND
- R5 pad 1: +3V3 -> SI_I2C_SDA_3V3
- R5 pad 2: PB2 -> +3V3
- R6 pad 1: VBUS -> SI_I2C_SCL_3V3
- R6 pad 2: Net-(U5-EN) -> +3V3
- U1 pad 1: (no net) -> SI_I2C_SDA_3V3
- U1 pad 2: (no net) -> GND
- U1 pad 3: (no net) -> unconnected-(U1-NC-Pad3)
- U1 pad 4: (no net) -> unconnected-(U1-NC-Pad4)
- U1 pad 5: (no net) -> +3V3
- U1 pad 6: GND -> SI_I2C_SCL_3V3
- U1 pad 7: +3V3 -> GND
- U2 pad 1: SDA0_3V3 -> +3V3
- U2 pad 2: GND -> Net-(U2-L2)
- U2 pad 3: unconnected-(U2-NC-Pad3) -> GND
- U2 pad 4: unconnected-(U2-NC-Pad4) -> Net-(U2-L1)
- U2 pad 5: +3V3 -> VBUS
- U2 pad 6: SCL0_3V3 -> Net-(U2-EN)
- U2 pad 7: GND -> Net-(U2-EN)
- U4 pad 1: PB5 -> /MCU/FLASH_SS
- U4 pad 2: PB3 -> /MCU/QSPI_SD1
- U4 pad 3: PB4 -> /MCU/QSPI_SD2
- U4 pad 5: PB0 -> /MCU/QSPI_SD0
- U4 pad 6: PB1 -> /MCU/QSPI_SCLK
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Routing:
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- added copper zone on F.Cu, net +1V1
- removed copper zone on F.Cu, net Net-(U5-EN)
- removed copper zone on F.Cu, net VBUS
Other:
- board text removed: "3V3 PB0 GND"
- board text removed: "PB1 PB2 PB5"

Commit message: finished routing up board, needs a double-check
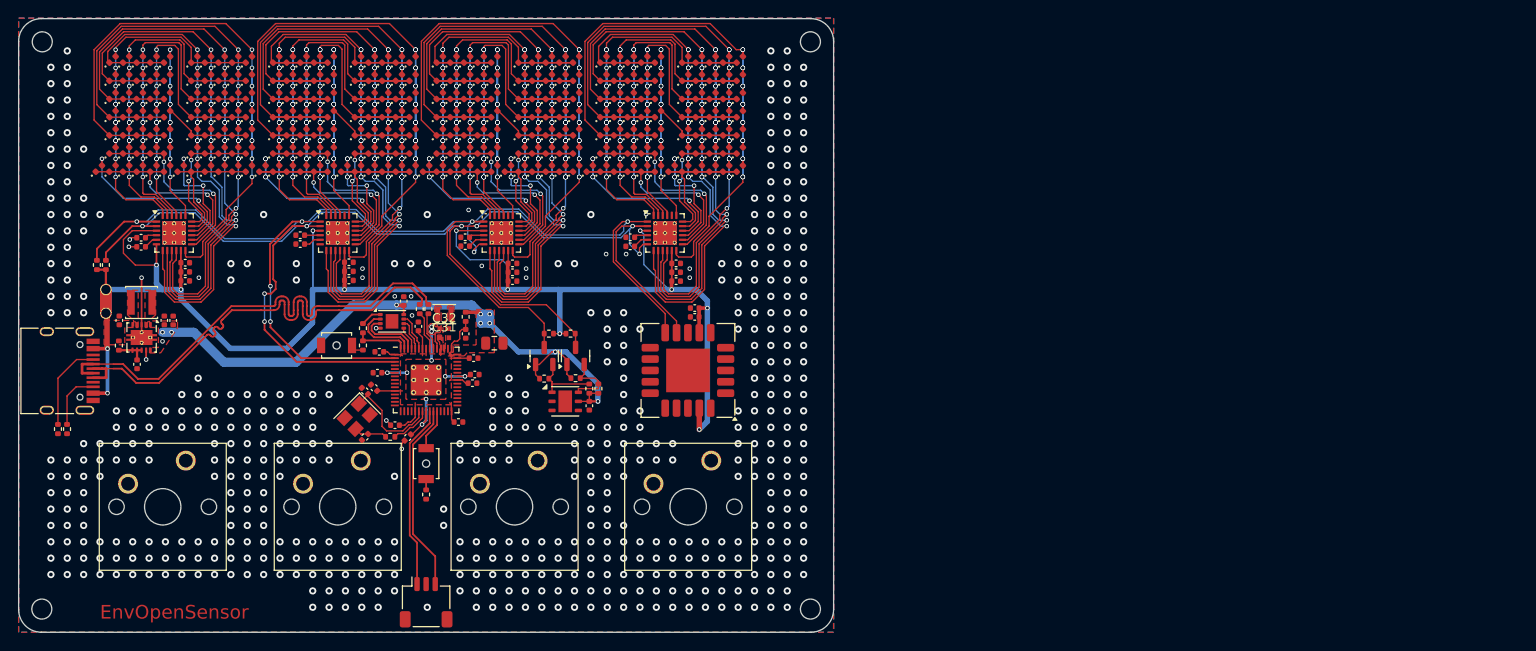
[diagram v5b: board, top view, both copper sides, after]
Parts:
- removed NT1: NetTie_2, NetTie:NetTie-2_THT_Pad1.0mm
- removed R11: 10K 0402, Resistor_SMD:R_0402_1005Metric
- C31, C32: footprint Capacitor_SMD:C_0402_1005Metric -> RP2350_60QFN_minimal:C_0402_1005Metric_small_pads
- moved R3 159.5 mm to (17.5, 57.6), turned to -90 degrees
- moved R4 158.0 mm to (18.5, 57.6), turned to -90 degrees
- moved R13 153.4 mm to (21.8, 39.6), turned to -90 degrees
- moved NT2 152.8 mm to (22.8, 44.9), turned to 90 degrees
- moved R12 152.7 mm to (22.8, 39.6), turned to -90 degrees
- moved C4 150.7 mm to (29.2, 45.7), turned to 90 degrees
- moved L1 149.7 mm to (26.7, 43.7)
- moved C5 149.4 mm to (30.2, 45.7), turned to 90 degrees
- moved R7 149.3 mm to (24.2, 48.5), turned to -90 degrees
- moved U2 145.7 mm to (26.7, 47.6), turned to -90 degrees
- moved C2 136.9 mm to (24.2, 45.7), turned to 90 degrees
- moved C3 134.9 mm to (26.2, 50.5), turned to -90 degrees
- moved C1 108.6 mm to (76.0, 55.1), turned to -90 degrees
- moved R8 107.5 mm to (71.5, 47.1)
- moved R5 105.5 mm to (71.0, 52.1), turned to 180 degrees
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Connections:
- C6 pad 1: +5V -> VCC
- C7 pad 1: +5V -> VCC
- R12 pad 2: +5V -> VCC
- R13 pad 2: +5V -> VCC
- R8 pad 2: +5V -> VCC
- R9 pad 2: +5V -> VCC
- U3 pad 19: +5V -> VCC
- U3 pad 7: +5V -> VCC
- U4 pad 9: GND -> (no net)
- U5 pad 2: /MCU/GPIO0 -> I2C_SDA_5V0
- U5 pad 3: /MCU/GPIO1 -> I2C_SCL_5V0
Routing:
- net I2C_SDA_5V0: track 6.86 -> 148.1 mm, vias 2 -> 7
- net I2C_SCL_5V0: track 6.98 -> 147.8 mm, vias 2 -> 8
- net +3V3: track 1.00 -> 96.8 mm, vias 0 -> 10
- net VCC: track 82.4 -> 172.1 mm, vias 5 -> 11
- net USB_D+: track 0.00 -> 53.6 mm
- net USB_D-: track 0.00 -> 53.3 mm
- net +1V1: track 5.81 -> 20.3 mm, vias 2 -> 9
- net VBUS: track 0.00 -> 12.0 mm, vias 0 -> 2
- net GND: track 1.87 -> 12.1 mm, vias 2 -> 542
- net Net-(J1-CC1): track 0.00 -> 9.81 mm
- net SI_I2C_SDA_3V3: track 0.00 -> 7.84 mm
- net SI_I2C_SCL_3V3: track 0.00 -> 7.24 mm
- net Net-(J1-CC2): track 0.00 -> 6.42 mm
- net Net-(U5-USB_DP): track 0.00 -> 4.31 mm
- net Net-(U5-USB_DM): track 0.00 -> 4.20 mm
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- added copper zone on F.Cu, net /MCU/VREG_LX
- added copper zone on F.Cu, net Net-(U2-L1)
- added copper zone on F.Cu, net Net-(U2-L2)
- added copper zone on F.Cu, net VBUS
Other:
- board text added: "3.3u"

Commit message: moved reset button - easier to access, added button labels, wired up switches
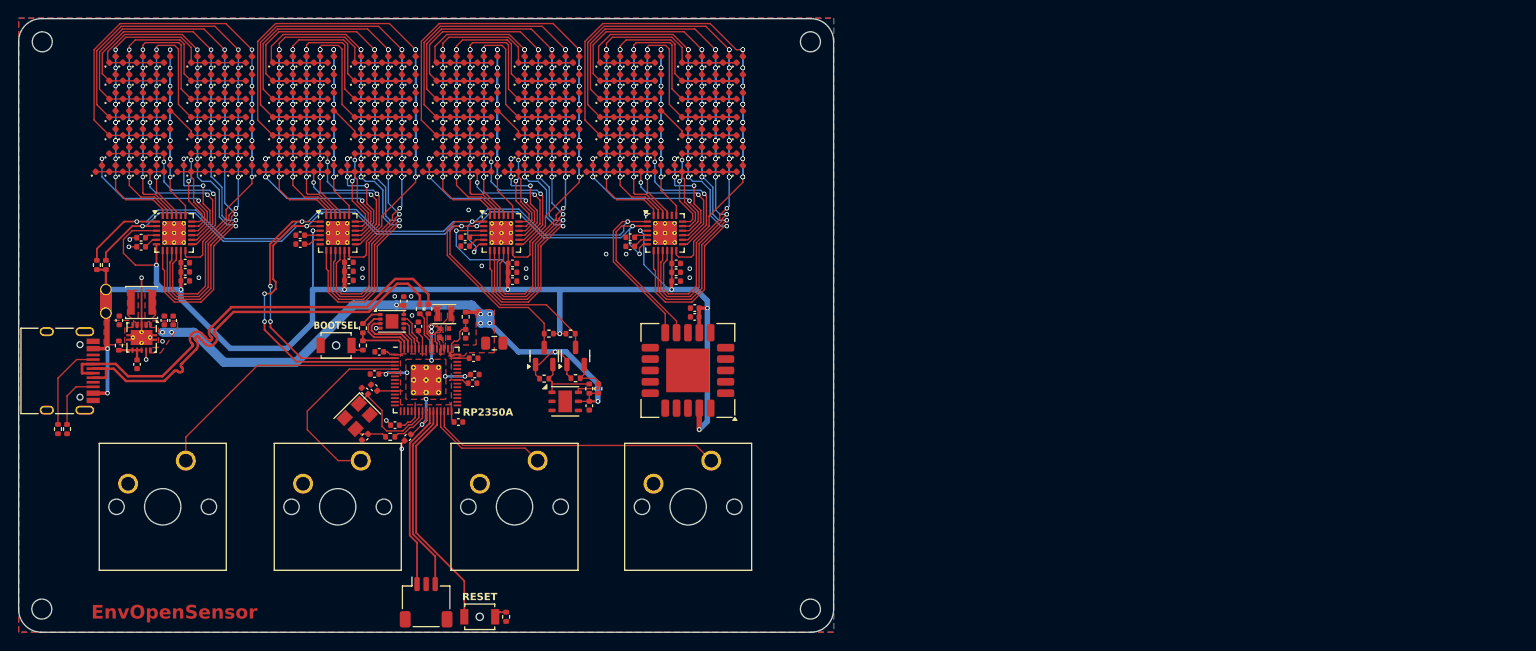
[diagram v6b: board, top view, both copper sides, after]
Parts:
- moved SW6 17.9 mm to (63.9, 78.3), turned to 180 degrees
- moved R26 16.1 mm to (66.8, 78.3)
- moved C33 0.36 mm to (52.3, 51.6)
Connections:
- U5 pad 27: /MCU/GPIO16 -> PB4
- U5 pad 28: /MCU/GPIO17 -> PB5
- U5 pad 4: /MCU/GPIO2 -> PB1
- U5 pad 5: /MCU/GPIO3 -> PB3
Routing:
- net PB5: track 0.00 -> 32.6 mm
- net PB1: track 0.00 -> 28.8 mm
- net /MCU/RUN: track 4.56 -> 25.8 mm
- net PB3: track 0.00 -> 20.9 mm
- net PB4: track 0.00 -> 13.9 mm
- net USB_D+: track 53.6 -> 49.9 mm
- net USB_D-: track 53.3 -> 49.9 mm
- net +1V1: track 20.3 -> 21.1 mm
- net GND: vias 542 -> 22
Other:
- board text added: "BOOTSEL"
- board text added: "RESET"
- board text added: "RP2350A"
